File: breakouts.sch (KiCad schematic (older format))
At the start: 28 parts, among them K5 CONN_3, P10 CONN_8, P11 CONN_5, P12 CONN_5, P13 CONN_6, P14 CONN_8, P15 CONN_5X2, P16 CONN_16, P17 CONN_16, P18 POWER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

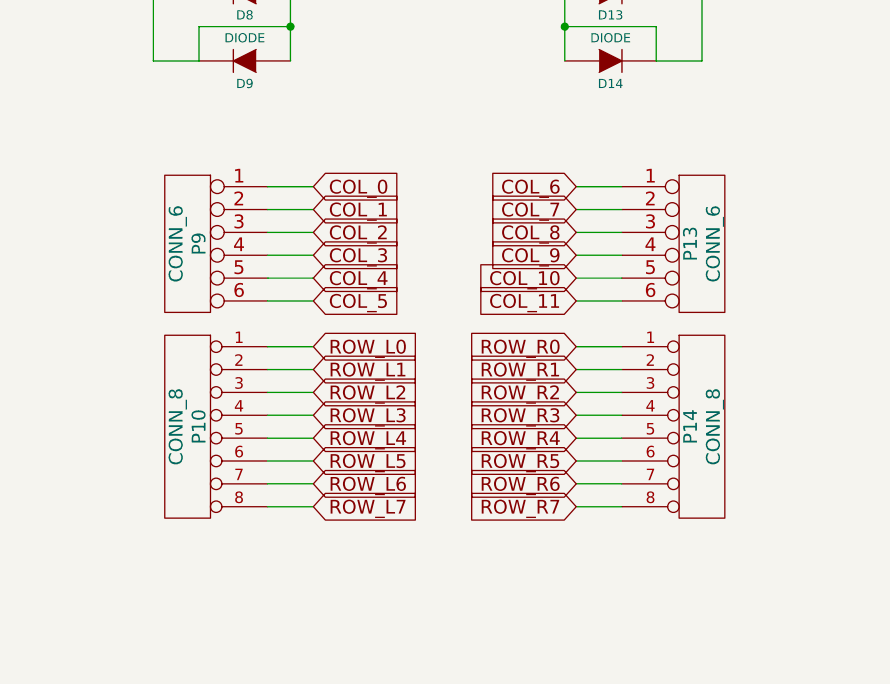
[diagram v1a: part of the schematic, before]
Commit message: Remove matrix breakout connectors
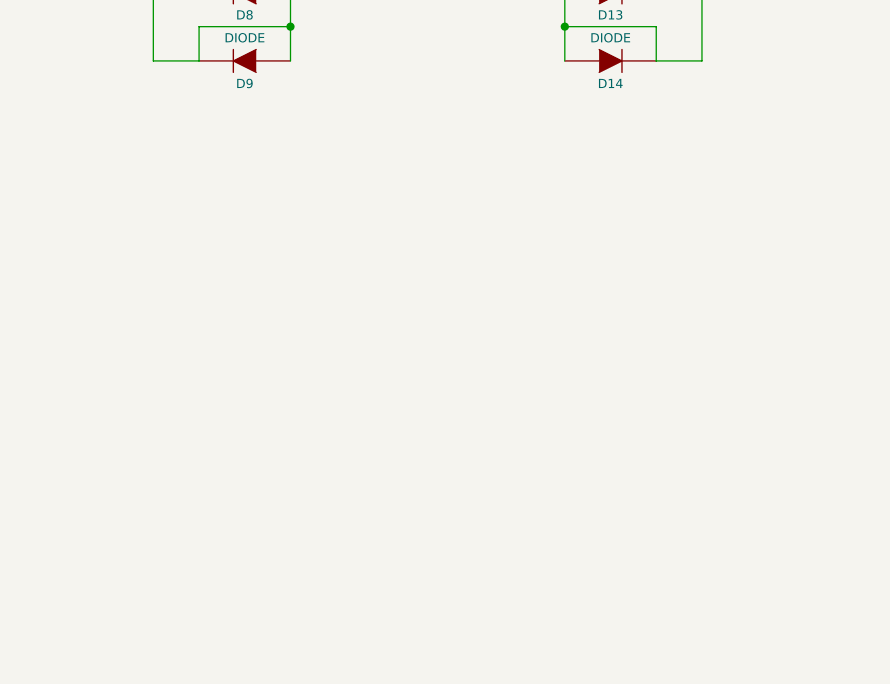
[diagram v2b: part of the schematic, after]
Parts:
- removed P10, P14: CONN_8, replacement_kinesis_controller:Pin_Header_Staggered_Straight_1x08, symbol CONN_8
- removed P13, P9: CONN_6, replacement_kinesis_controller:Pin_Header_Staggered_Straight_1x06, symbol CONN_6
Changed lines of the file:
@@
 Comment4 ""
 $EndDescr
-Text GLabel 2800 3650 2    60   Input ~ 0
-ROW_L0
-Text GLabel 2800 3750 2    60   Input ~ 0
-ROW_L1
-Text GLabel 2800 3850 2    60   Input ~ 0
-ROW_L2
-Text GLabel 2800 3950 2    60   Input ~ 0
-ROW_L3
-Text GLabel 2800 4050 2    60   Input ~ 0
-ROW_L4
-Text GLabel 2800 4150 2    60   Input ~ 0
-ROW_L5
-Text GLabel 2800 4250 2    60   Input ~ 0
-ROW_L6
-Text GLabel 2800 4350 2    60   Input ~ 0
-ROW_L7
-Text GLabel 3950 3650 0    60   Input ~ 0
-ROW_R0
-Text GLabel 3950 3750 0    60   Input ~ 0
-ROW_R1
-Text GLabel 3950 3850 0    60   Input ~ 0
-ROW_R2
-Text GLabel 3950 3950 0    60   Input ~ 0
-ROW_R3
-Text GLabel 3950 4050 0    60   Input ~ 0
-ROW_R4
-Text GLabel 3950 4150 0    60   Input ~ 0
-ROW_R5
-Text GLabel 3950 4250 0    60   Input ~ 0
-ROW_R6
-Text GLabel 3950 4350 0    60   Input ~ 0
-ROW_R7
-Text GLabel 2800 2950 2    60   Input ~ 0
-COL_0
-Text GLabel 2800 3050 2    60   Input ~ 0
-COL_1
-Text GLabel 2800 3150 2    60   Input ~ 0
-COL_2
-Text GLabel 2800 3250 2    60   Input ~ 0
-COL_3
-Text GLabel 2800 3350 2    60   Input ~ 0
-COL_4
-Text GLabel 2800 3450 2    60   Input ~ 0
-COL_5
-Text GLabel 3950 2950 0    60   Input ~ 0
-COL_6
-Text GLabel 3950 3050 0    60   Input ~ 0
-COL_7
-Text GLabel 3950 3150 0    60   Input ~ 0
-COL_8
-Text GLabel 3950 3250 0    60   Input ~ 0
-COL_9
-Text GLabel 3950 3350 0    60   Input ~ 0
-COL_10
-Text GLabel 3950 3450 0    60   Input ~ 0
-COL_11
-$Comp
-L CONN_6 P13
-U 1 1 54E55166
-P 4500 3200
-F 0 "P13" V 4450 3200 60  0000 C CNN
-F 1 "CONN_6" V 4550 3200 60  0000 C CNN
-F 2 "replacement_kinesis_controller:Pin_Header_Staggered_Straight_1x06" H 4500 3200 60  0001 C CNN
-F 3 "" H 4500 3200 60  0000 C CNN
-	1    4500 3200
-	1    0    0    -1
-$EndComp
-$Comp
-L CONN_6 P9
-U 1 1 54E5516D
-P 2250 3200
-F 0 "P9" V 2200 3200 60  0000 C CNN
-F 1 "CONN_6" V 2300 3200 60  0000 C CNN
-F 2 "replacement_kinesis_controller:Pin_Header_Staggered_Straight_1x06" H 2250 3200 60  0001 C CNN
-F 3 "" H 2250 3200 60  0000 C CNN
-	1    2250 3200
-	-1   0    0    -1
-$EndComp
-$Comp
-L CONN_8 P14
-U 1 1 54E55174
-P 4500 4000
-F 0 "P14" V 4450 4000 60  0000 C CNN
-F 1 "CONN_8" V 4550 4000 60  0000 C CNN
-F 2 "replacement_kinesis_controller:Pin_Header_Staggered_Straight_1x08" H 4500 4000 60  0001 C CNN
-F 3 "" H 4500 4000 60  0000 C CNN
-	1    4500 4000
-	1    0    0    -1
-$EndComp
-$Comp
-L CONN_8 P10
-U 1 1 54E5517B
-P 2250 4000
-F 0 "P10" V 2200 4000 60  0000 C CNN
-F 1 "CONN_8" V 2300 4000 60  0000 C CNN
-F 2 "replacement_kinesis_controller:Pin_Header_Staggered_Straight_1x08" H 2250 4000 60  0001 C CNN
-F 3 "" H 2250 4000 60  0000 C CNN
-	1    2250 4000
-	-1   0    0    -1
-$EndComp
-Wire Wire Line
-	2600 2950 2800 2950
-Wire Wire Line
-	2600 3050 2800 3050
-Wire Wire Line
-	2600 3150 2800 3150
-Wire Wire Line
-	2600 3250 2800 3250
-Wire Wire Line
-	2600 3350 2800 3350
-Wire Wire Line
-	2600 3450 2800 3450
-Wire Wire Line
-	2600 3650 2800 3650
-Wire Wire Line
-	2600 3750 2800 3750
-Wire Wire Line
-	2600 3850 2800 3850
-Wire Wire Line
-	2600 3950 2800 3950
-Wire Wire Line
-	2600 4050 2800 4050
-Wire Wire Line
-	2800 4150 2600 4150
-Wire Wire Line
-	2600 4250 2800 4250
-Wire Wire Line
-	2800 4350 2600 4350
-Wire Wire Line
-	3950 4350 4150 4350
-Wire Wire Line
-	4150 4250 3950 4250
-Wire Wire Line
-	3950 4150 4150 4150
-Wire Wire Line
-	4150 4050 3950 4050
-Wire Wire Line
-	3950 3950 4150 3950
-Wire Wire Line
-	4150 3850 3950 3850
-Wire Wire Line
-	3950 3750 4150 3750
-Wire Wire Line
-	3950 3650 4150 3650
-Wire Wire Line
-	4150 3450 3950 3450
-Wire Wire Line
-	3950 3350 4150 3350
-Wire Wire Line
-	4150 3250 3950 3250
-Wire Wire Line
-	3950 3150 4150 3150
-Wire Wire Line
-	4150 3050 3950 3050
-Wire Wire Line
-	3950 2950 4150 2950
 Text GLabel 2850 6200 0    60   BiDi ~ 0
 SCL
